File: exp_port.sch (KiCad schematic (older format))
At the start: 4 parts, among them CN1 EXPANSION_CONNECTOR

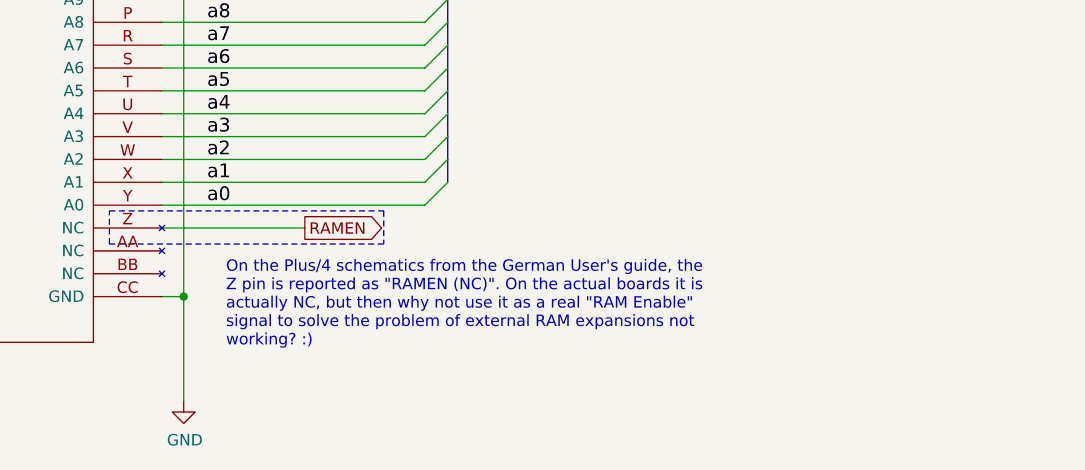
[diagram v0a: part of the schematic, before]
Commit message: Add jumper on RAMEN
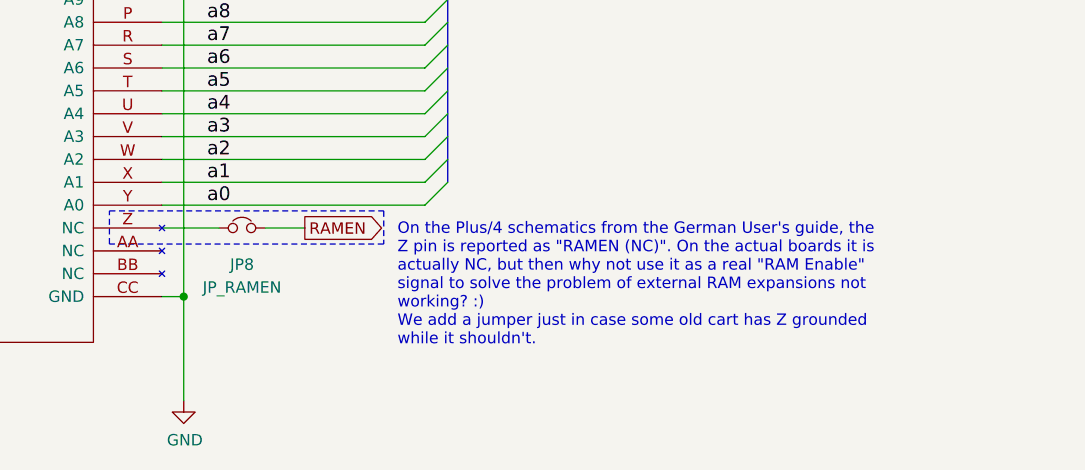
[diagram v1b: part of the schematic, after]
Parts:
- added JP8: JP_RAMEN, Jumper:SolderJumper-2_P1.3mm_Open_RoundedPad1.0x1.5mm, symbol Device:Jumper_NC_Small
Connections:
- net RAMEN: now also JP8.2; no longer CN1.Z (NC)
- new net: CN1.Z (NC), JP8.1
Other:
- note added: "On the Plus/4 schematics from the German User's guide, the\nZ pin is reported as "RAMEN (NC)". On the actual boards it is\nactually NC, but then why not use it as a real "RAM Enable"\nsignal to solve the problem of external RAM expansions not\nworking? :)\nWe add a jumper just in case some old cart has Z grounded\nwhile it shouldn't."
- note removed: "On the Plus/4 schematics from the German User's guide, the\nZ pin is reported as "RAMEN (NC)". On the actual boards it is\nactually NC, but then why not use it as a real "RAM Enable"\nsignal to solve the problem of external RAM expansions not\nworking? :)"
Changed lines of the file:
@@
 RAMEN
 Wire Wire Line
-	6605 5190 7230 5190
+	6605 5190 6855 5190
 Wire Notes Line
 	6375 5115 7575 5115
@@
 Wire Notes Line
 	6375 5260 6375 5115
-Text Notes 6885 5715 0    50   ~ 0
-On the Plus/4 schematics from the German User's guide, the\nZ pin is reported as "RAMEN (NC)". On the actual boards it is\nactually NC, but then why not use it as a real "RAM Enable"\nsignal to solve the problem of external RAM expansions not\nworking? :)
+Text Notes 7635 5710 0    50   ~ 0
+On the Plus/4 schematics from the German User's guide, the\nZ pin is reported as "RAMEN (NC)". On the actual boards it is\nactually NC, but then why not use it as a real "RAM Enable"\nsignal to solve the problem of external RAM expansions not\nworking? :)\nWe add a jumper just in case some old cart has Z grounded\nwhile it shouldn't.
 Wire Bus Line
 	3910 4290 3910 4990
 Wire Bus Line
 	7855 3490 7855 4990
+$Comp
+L Device:Jumper_NC_Small JP8
+U 1 1 61F43269
+P 6955 5190
+F 0 "JP8" H 6955 5030 50  0000 C CNN
+F 1 "JP_RAMEN" H 6955 4930 50  0000 C CNN
+F 2 "Jumper:SolderJumper-2_P1.3mm_Open_RoundedPad1.0x1.5mm" H 6955 5190 50  0001 C CNN
+F 3 "~" H 6955 5190 50  0001 C CNN
+	1    6955 5190
+	1    0    0    -1
+$EndComp
+Wire Wire Line
+	7055 5190 7230 5190
 $EndSCHEMATC

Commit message: Close JP8 by default
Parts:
- JP8: footprint Jumper:SolderJumper-2_P1.3mm_Open_RoundedPad1.0x1.5mm -> Jumper:SolderJumper-2_P1.3mm_Bridged_RoundedPad1.0x1.5mm
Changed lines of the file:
@@
 F 0 "JP8" H 6955 5030 50  0000 C CNN
 F 1 "JP_RAMEN" H 6955 4930 50  0000 C CNN
-F 2 "Jumper:SolderJumper-2_P1.3mm_Open_RoundedPad1.0x1.5mm" H 6955 5190 50  0001 C CNN
+F 2 "Jumper:SolderJumper-2_P1.3mm_Bridged_RoundedPad1.0x1.5mm" H 6955 5190 50  0001 C CNN
 F 3 "~" H 6955 5190 50  0001 C CNN
 	1    6955 5190

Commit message: Add C94 and C95, remove C108
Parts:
- added C94: 100n/25V, Capacitor_THT:C_Disc_D8.0mm_W2.5mm_P5.00mm, symbol Device:C
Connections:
- net GND: now also C94.2
- net VCC: now also C94.1
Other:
- note added: "Additional\ndecoupling cap"
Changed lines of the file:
@@
 Sheet 8 12
 Title "LittleSixteen"
-Date "2020-01-03"
+Date "2021-12-05"
 Rev "3git"
 Comp "SukkoPera"
@@
 Wire Wire Line
 	7055 5190 7230 5190
+Wire Wire Line
+	10280 3965 10280 3900
+$Comp
+L Device:C C?
+U 1 1 6349BFDB
+P 10280 4115
+AR Path="/5EACE220/6349BFDB" Ref="C?"  Part="1"
+AR Path="/5E6A379E/6349BFDB" Ref="C94"  Part="1"
+F 0 "C94" H 10395 4161 50  0000 L CNN
+F 1 "100n/25V" H 10395 4070 50  0000 L CNN
+F 2 "Capacitor_THT:C_Disc_D8.0mm_W2.5mm_P5.00mm" H 10318 3965 50  0001 C CNN
+F 3 "~" H 10280 4115 50  0001 C CNN
+	1    10280 4115
+	1    0    0    -1
+$EndComp
+Wire Wire Line
+	10280 4265 10280 4325
+$Comp
+L power:VCC #PWR0149
+U 1 1 6349D8C1
+P 10280 3900
+F 0 "#PWR0149" H 10280 3750 50  0001 C CNN
+F 1 "VCC" H 10297 4073 50  0000 C CNN
+F 2 "" H 10280 3900 50  0001 C CNN
+F 3 "" H 10280 3900 50  0001 C CNN
+	1    10280 3900
+	1    0    0    -1
+$EndComp
+$Comp
+L power:GND #PWR0150
+U 1 1 6349E0F9
+P 10280 4325
+F 0 "#PWR0150" H 10280 4075 50  0001 C CNN
+F 1 "GND" H 10285 4152 50  0000 C CNN
+F 2 "" H 10280 4325 50  0001 C CNN
+F 3 "" H 10280 4325 50  0001 C CNN
+	1    10280 4325
+	1    0    0    -1
+$EndComp
+Text Notes 10045 4725 0    50   ~ 0
+Additional\ndecoupling cap
 Wire Bus Line
 	3910 4290 3910 4990

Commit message: Use local Ferrite_Bead_Small symbol
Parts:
- FB38, FB39, FB40: symbol Device:Ferrite_Bead_Small -> ferrite_bead_small:Ferrite_Bead_Small
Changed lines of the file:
@@
 	6700 5490 6700 3090
 $Comp
-L Device:Ferrite_Bead_Small FB38
+L ferrite_bead_small:Ferrite_Bead_Small FB38
 U 1 1 5E9793EF
 P 6905 3390
@@
 	6805 3390 6605 3390
 $Comp
-L Device:Ferrite_Bead_Small FB40
+L ferrite_bead_small:Ferrite_Bead_Small FB40
 U 1 1 5E979856
 P 4765 4090
@@
 	7440 3490 7205 3490
 $Comp
-L Device:Ferrite_Bead_Small FB39
+L ferrite_bead_small:Ferrite_Bead_Small FB39
 U 1 1 5E982F3B
 P 7105 3490

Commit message: Add userport schematics and enlarge board
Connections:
- net ~RESET renamed ~BRESET
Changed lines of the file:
@@
 $Descr A4 11693 8268
 encoding utf-8
-Sheet 8 12
+Sheet 8 13
 Title "LittleSixteen"
 Date "2021-12-05"
@@
 	6605 3290 7440 3290
 Text GLabel 7440 3290 2    50   Input ~ 0
-~RESET
+~BRESET
 Text GLabel 7230 3190 2    50   Input ~ 0
 C1_LOW

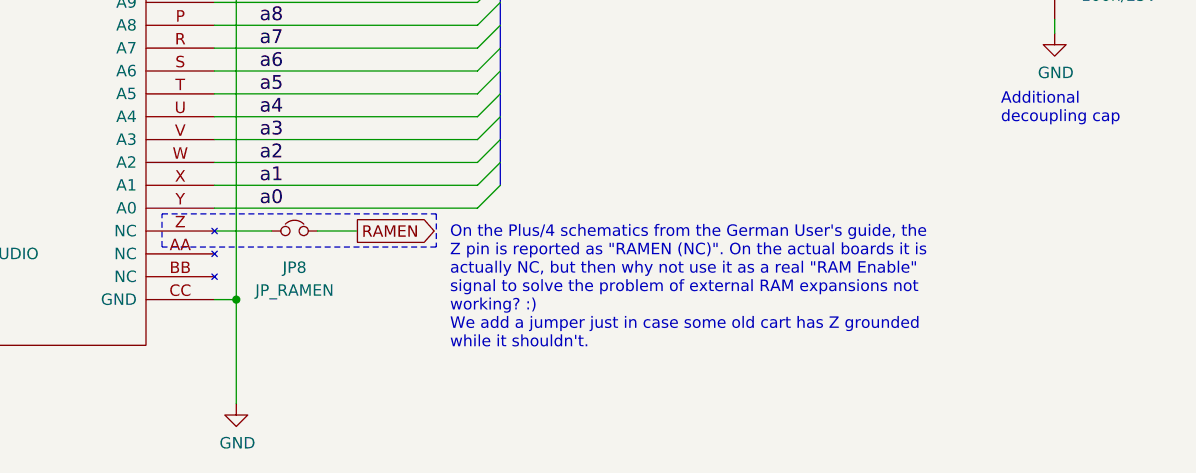
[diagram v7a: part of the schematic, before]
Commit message: Add 512kB RAM expansions, Hannes-style
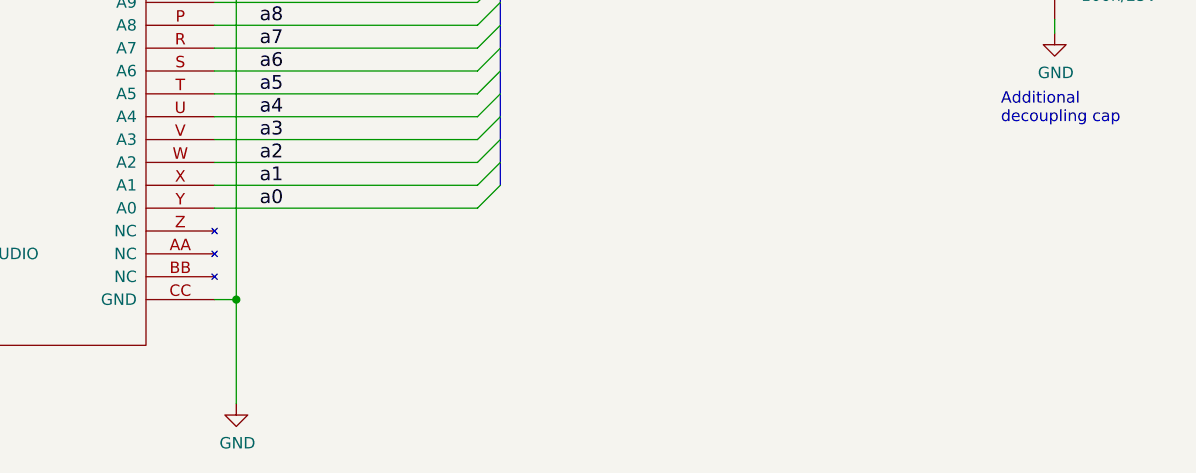
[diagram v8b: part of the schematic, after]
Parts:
- removed JP8: JP_RAMEN, Jumper:SolderJumper-2_P1.3mm_Bridged_RoundedPad1.0x1.5mm, symbol Device:Jumper_NC_Small
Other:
- note removed: "On the Plus/4 schematics from the German User's guide, the\nZ pin is reported as "RAMEN (NC)". On the actual boards it is\nactually NC, but then why not use it as a real "RAM Enable"\nsignal to solve the problem of external RAM expansions not\nworking? :)\nWe add a jumper just in case some old cart has Z grounded\nwhile it shouldn't."
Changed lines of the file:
@@
 Text GLabel 4570 3490 0    50   Input ~ 0
 R_~W
-$Comp
-L Exp-Port:C16-Exp-Port CN1
-U 1 1 5E91CB40
-P 5855 4290
-F 0 "CN1" H 5855 5855 50  0000 C CNN
-F 1 "EXPANSION_CONNECTOR" H 5855 5764 50  0000 C CNN
-F 2 "LittleSixteen:50Pin_Edge_Connector" H 5855 2640 50  0001 C CNN
-F 3 "DOCUMENTATION" H 5855 2540 50  0001 C CNN
-	1    5855 4290
-	1    0    0    -1
-$EndComp
 Text Label 6905 5090 2    60   ~ 0
 a0
@@
 Wire Wire Line
 	4580 5290 5105 5290
-Text GLabel 7230 5190 2    50   Output ~ 0
-RAMEN
-Wire Wire Line
-	6605 5190 6855 5190
-Wire Notes Line
-	6375 5115 7575 5115
-Wire Notes Line
-	7575 5115 7575 5260
-Wire Notes Line
-	7575 5260 6375 5260
-Wire Notes Line
-	6375 5260 6375 5115
-Text Notes 7635 5710 0    50   ~ 0
-On the Plus/4 schematics from the German User's guide, the\nZ pin is reported as "RAMEN (NC)". On the actual boards it is\nactually NC, but then why not use it as a real "RAM Enable"\nsignal to solve the problem of external RAM expansions not\nworking? :)\nWe add a jumper just in case some old cart has Z grounded\nwhile it shouldn't.
-$Comp
-L Device:Jumper_NC_Small JP8
-U 1 1 61F43269
-P 6955 5190
-F 0 "JP8" H 6955 5030 50  0000 C CNN
-F 1 "JP_RAMEN" H 6955 4930 50  0000 C CNN
-F 2 "Jumper:SolderJumper-2_P1.3mm_Bridged_RoundedPad1.0x1.5mm" H 6955 5190 50  0001 C CNN
-F 3 "~" H 6955 5190 50  0001 C CNN
-	1    6955 5190
-	1    0    0    -1
-$EndComp
-Wire Wire Line
-	7055 5190 7230 5190
 Wire Wire Line
 	10280 3965 10280 3900
@@
 Text Notes 10045 4725 0    50   ~ 0
 Additional\ndecoupling cap
+$Comp
+L Exp-Port:C16-Exp-Port CN1
+U 1 1 5E91CB40
+P 5855 4290
+F 0 "CN1" H 5855 5855 50  0000 C CNN
+F 1 "EXPANSION_CONNECTOR" H 5855 5764 50  0000 C CNN
+F 2 "LittleSixteen:50Pin_Edge_Connector" H 5855 2640 50  0001 C CNN
+F 3 "DOCUMENTATION" H 5855 2540 50  0001 C CNN
+	1    5855 4290
+	1    0    0    -1
+$EndComp
 Wire Bus Line
 	3910 4290 3910 4990
